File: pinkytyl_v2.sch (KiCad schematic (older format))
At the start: 62 parts, among them J1 50-00174, J2 Conn_01x02, J3 USB_B_Mini, J5 Conn_02x05_Odd_Even, K0 KEYSW, K10 KEYSW, K11 KEYSW, K12 KEYSW, K13 KEYSW, K14 KEYSW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

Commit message: Initial commit for chocs
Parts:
- added D1: D, Diode_SMD:D_SOD-123, symbol Device:D
- K0, K10, K11, K12, K13, K14, K15, K20, K21, K22, K23, K24, K25, K30, K31, K32, K33, K34, K35, K40, K41: footprint keyswitches:SW_MX_reversible_minimal -> keyswitches:SW_PG1350_reversible
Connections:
- net GND: now also U1.33 (~HWB~/PE2)
- net VCC: now also D1.1 (K); no longer J3.1 (VBUS), U1.7 (VBUS)
- new net UVCC: D1.2 (A), J3.1 (VBUS), U1.7 (VBUS)
- no-connect marks 20 -> 19
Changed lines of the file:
@@
-$EndComp
-$Comp
-L power:VCC #PWR0105
-U 1 1 614864FA
-P 2300 2000
-F 0 "#PWR0105" H 2300 1850 50  0001 C CNN
-F 1 "VCC" V 2300 2150 50  0000 L CNN
-F 2 "" H 2300 2000 50  0001 C CNN
-F 3 "" H 2300 2000 50  0001 C CNN
-	1    2300 2000
-	0    -1   -1   0
 $EndComp
 $Comp
@@
 NoConn ~ 3500 2900
 NoConn ~ 3500 3000
-NoConn ~ 3500 3300
 NoConn ~ 3500 3600
 NoConn ~ 3500 3700
@@
 F 0 "K10" H 5550 4133 60  0000 C CNN
 F 1 "KEYSW" H 5550 3800 60  0001 C CNN
-F 2 "keyswitches:SW_MX_reversible_minimal" H 5550 3900 60  0001 C CNN
+F 2 "keyswitches:SW_PG1350_reversible" H 5550 3900 60  0001 C CNN
 F 3 "" H 5550 3900 60  0000 C CNN
 	1    5550 3900
@@
 F 0 "K11" H 6450 4133 60  0000 C CNN
 F 1 "KEYSW" H 6450 3800 60  0001 C CNN
-F 2 "keyswitches:SW_MX_reversible_minimal" H 6450 3900 60  0001 C CNN
+F 2 "keyswitches:SW_PG1350_reversible" H 6450 3900 60  0001 C CNN
 F 3 "" H 6450 3900 60  0000 C CNN
 	1    6450 3900
@@
 F 0 "K12" H 7350 4133 60  0000 C CNN
 F 1 "KEYSW" H 7350 3800 60  0001 C CNN
-F 2 "keyswitches:SW_MX_reversible_minimal" H 7350 3900 60  0001 C CNN
+F 2 "keyswitches:SW_PG1350_reversible" H 7350 3900 60  0001 C CNN
 F 3 "" H 7350 3900 60  0000 C CNN
 	1    7350 3900
@@
 F 0 "K13" H 8200 4133 60  0000 C CNN
 F 1 "KEYSW" H 8200 3800 60  0001 C CNN
-F 2 "keyswitches:SW_MX_reversible_minimal" H 8200 3900 60  0001 C CNN
+F 2 "keyswitches:SW_PG1350_reversible" H 8200 3900 60  0001 C CNN
 F 3 "" H 8200 3900 60  0000 C CNN
 	1    8200 3900
@@
 F 0 "K14" H 9050 4133 60  0000 C CNN
 F 1 "KEYSW" H 9050 3800 60  0001 C CNN
-F 2 "keyswitches:SW_MX_reversible_minimal" H 9050 3900 60  0001 C CNN
+F 2 "keyswitches:SW_PG1350_reversible" H 9050 3900 60  0001 C CNN
 F 3 "" H 9050 3900 60  0000 C CNN
 	1    9050 3900
@@
 F 0 "K15" H 10000 4133 60  0000 C CNN
 F 1 "KEYSW" H 10000 3800 60  0001 C CNN
-F 2 "keyswitches:SW_MX_reversible_minimal" H 10000 3900 60  0001 C CNN
+F 2 "keyswitches:SW_PG1350_reversible" H 10000 3900 60  0001 C CNN
 F 3 "" H 10000 3900 60  0000 C CNN
 	1    10000 3900
@@
 F 0 "K20" H 5550 4883 60  0000 C CNN
 F 1 "KEYSW" H 5550 4550 60  0001 C CNN
-F 2 "keyswitches:SW_MX_reversible_minimal" H 5550 4650 60  0001 C CNN
+F 2 "keyswitches:SW_PG1350_reversible" H 5550 4650 60  0001 C CNN
 F 3 "" H 5550 4650 60  0000 C CNN
 	1    5550 4650
@@
 F 0 "K21" H 6450 4883 60  0000 C CNN
 F 1 "KEYSW" H 6450 4550 60  0001 C CNN
-F 2 "keyswitches:SW_MX_reversible_minimal" H 6450 4650 60  0001 C CNN
+F 2 "keyswitches:SW_PG1350_reversible" H 6450 4650 60  0001 C CNN
 F 3 "" H 6450 4650 60  0000 C CNN
 	1    6450 4650
@@
 F 0 "K22" H 7350 4883 60  0000 C CNN
 F 1 "KEYSW" H 7350 4550 60  0001 C CNN
-F 2 "keyswitches:SW_MX_reversible_minimal" H 7350 4650 60  0001 C CNN
+F 2 "keyswitches:SW_PG1350_reversible" H 7350 4650 60  0001 C CNN
 F 3 "" H 7350 4650 60  0000 C CNN
 	1    7350 4650
@@
 F 0 "K23" H 8200 4883 60  0000 C CNN
 F 1 "KEYSW" H 8200 4550 60  0001 C CNN
-F 2 "keyswitches:SW_MX_reversible_minimal" H 8200 4650 60  0001 C CNN
+F 2 "keyswitches:SW_PG1350_reversible" H 8200 4650 60  0001 C CNN
 F 3 "" H 8200 4650 60  0000 C CNN
 	1    8200 4650
@@
 F 0 "K24" H 9050 4883 60  0000 C CNN
 F 1 "KEYSW" H 9050 4550 60  0001 C CNN
-F 2 "keyswitches:SW_MX_reversible_minimal" H 9050 4650 60  0001 C CNN
+F 2 "keyswitches:SW_PG1350_reversible" H 9050 4650 60  0001 C CNN
 F 3 "" H 9050 4650 60  0000 C CNN
 	1    9050 4650
@@
 F 0 "K25" H 10000 4883 60  0000 C CNN
 F 1 "KEYSW" H 10000 4550 60  0001 C CNN
-F 2 "keyswitches:SW_MX_reversible_minimal" H 10000 4650 60  0001 C CNN
+F 2 "keyswitches:SW_PG1350_reversible" H 10000 4650 60  0001 C CNN
 F 3 "" H 10000 4650 60  0000 C CNN
 	1    10000 4650
@@
 F 0 "K30" H 5550 5683 60  0000 C CNN
 F 1 "KEYSW" H 5550 5350 60  0001 C CNN
-F 2 "keyswitches:SW_MX_reversible_minimal" H 5550 5450 60  0001 C CNN
+F 2 "keyswitches:SW_PG1350_reversible" H 5550 5450 60  0001 C CNN
 F 3 "" H 5550 5450 60  0000 C CNN
 	1    5550 5450
@@
 F 0 "K31" H 6450 5683 60  0000 C CNN
 F 1 "KEYSW" H 6450 5350 60  0001 C CNN
-F 2 "keyswitches:SW_MX_reversible_minimal" H 6450 5450 60  0001 C CNN
+F 2 "keyswitches:SW_PG1350_reversible" H 6450 5450 60  0001 C CNN
 F 3 "" H 6450 5450 60  0000 C CNN
 	1    6450 5450
@@
 F 0 "K32" H 7350 5683 60  0000 C CNN
 F 1 "KEYSW" H 7350 5350 60  0001 C CNN
-F 2 "keyswitches:SW_MX_reversible_minimal" H 7350 5450 60  0001 C CNN
+F 2 "keyswitches:SW_PG1350_reversible" H 7350 5450 60  0001 C CNN
 F 3 "" H 7350 5450 60  0000 C CNN
 	1    7350 5450
@@
 F 0 "K33" H 8200 5683 60  0000 C CNN
 F 1 "KEYSW" H 8200 5350 60  0001 C CNN
-F 2 "keyswitches:SW_MX_reversible_minimal" H 8200 5450 60  0001 C CNN
+F 2 "keyswitches:SW_PG1350_reversible" H 8200 5450 60  0001 C CNN
 F 3 "" H 8200 5450 60  0000 C CNN
 	1    8200 5450
@@
 F 0 "K34" H 9050 5683 60  0000 C CNN
 F 1 "KEYSW" H 9050 5350 60  0001 C CNN
-F 2 "keyswitches:SW_MX_reversible_minimal" H 9050 5450 60  0001 C CNN
+F 2 "keyswitches:SW_PG1350_reversible" H 9050 5450 60  0001 C CNN
 F 3 "" H 9050 5450 60  0000 C CNN
 	1    9050 5450
@@
 F 0 "K35" H 10000 5683 60  0000 C CNN
 F 1 "KEYSW" H 10000 5350 60  0001 C CNN
-F 2 "keyswitches:SW_MX_reversible_minimal" H 10000 5450 60  0001 C CNN
+F 2 "keyswitches:SW_PG1350_reversible" H 10000 5450 60  0001 C CNN
 F 3 "" H 10000 5450 60  0000 C CNN
 	1    10000 5450
@@
 F 0 "K40" H 9050 6383 60  0000 C CNN
 F 1 "KEYSW" H 9050 6050 60  0001 C CNN
-F 2 "keyswitches:SW_MX_reversible_minimal" H 9050 6150 60  0001 C CNN
+F 2 "keyswitches:SW_PG1350_reversible" H 9050 6150 60  0001 C CNN
 F 3 "" H 9050 6150 60  0000 C CNN
 	1    9050 6150
@@
 F 0 "K41" H 10000 6383 60  0000 C CNN
 F 1 "KEYSW" H 10000 6050 60  0001 C CNN
-F 2 "keyswitches:SW_MX_reversible_minimal" H 10000 6150 60  0001 C CNN
+F 2 "keyswitches:SW_PG1350_reversible" H 10000 6150 60  0001 C CNN
 F 3 "" H 10000 6150 60  0000 C CNN
 	1    10000 6150
@@
 F 0 "K0" H 6450 3483 60  0000 C CNN
 F 1 "KEYSW" H 6450 3150 60  0001 C CNN
-F 2 "keyswitches:SW_MX_reversible_minimal" H 6450 3250 60  0001 C CNN
+F 2 "keyswitches:SW_PG1350_reversible" H 6450 3250 60  0001 C CNN
 F 3 "" H 6450 3250 60  0000 C CNN
 	1    6450 3250
@@
 	1    0    0    -1
 $EndComp
-$Comp
-L power:VCC #PWR0109
-U 1 1 614BD830
-P 5350 850
-F 0 "#PWR0109" H 5350 700 50  0001 C CNN
-F 1 "VCC" V 5365 978 50  0000 L CNN
-F 2 "" H 5350 850 50  0001 C CNN
-F 3 "" H 5350 850 50  0001 C CNN
-	1    5350 850
-	0    1    1    0
-$EndComp
 NoConn ~ 5350 1250
 $Comp
@@
 Connection ~ 2900 800
 Wire Wire Line
-	2800 900  2800 800
-Wire Wire Line
-	2800 800  2900 800
-Wire Wire Line
 	950  1300 950  1200
 Connection ~ 950  1200
@@
 	1    0    0    -1
 $EndComp
+$Comp
+L power:GND #PWR06
+U 1 1 616DF351
+P 3500 3300
+F 0 "#PWR06" H 3500 3050 50  0001 C CNN
+F 1 "GND" V 3505 3172 50  0000 R CNN
+F 2 "" H 3500 3300 50  0001 C CNN
+F 3 "" H 3500 3300 50  0001 C CNN
+	1    3500 3300
+	0    -1   -1   0
+$EndComp
+$Comp
+L Device:D D1
+U 1 1 61713DAC
+P 5550 650
+F 0 "D1" H 5400 750 50  0000 L CNN
+F 1 "D" H 5595 730 50  0000 L CNN
+F 2 "Diode_SMD:D_SOD-123" H 5550 650 50  0001 C CNN
+F 3 "~" H 5550 650 50  0001 C CNN
+F 4 "C81598" H 5550 650 50  0001 C CNN "LCSC"
+	1    5550 650
+	-1   0    0    1
+$EndComp
+Text GLabel 5500 850  2    50   Input ~ 0
+UVCC
+Wire Wire Line
+	5500 850  5400 850
+Wire Wire Line
+	5400 650  5400 850
+Connection ~ 5400 850
+Wire Wire Line
+	5400 850  5350 850
+Wire Wire Line
+	2800 900  2800 800
+Wire Wire Line
+	2800 800  2900 800
+Text GLabel 2300 2000 0    50   Input ~ 0
+UVCC
+$Comp
+L power:VCC #PWR0105
+U 1 1 61762081
+P 5700 650
+F 0 "#PWR0105" H 5700 500 50  0001 C CNN
+F 1 "VCC" H 5715 823 50  0000 C CNN
+F 2 "" H 5700 650 50  0001 C CNN
+F 3 "" H 5700 650 50  0001 C CNN
+	1    5700 650
+	0    1    1    0
+$EndComp
 $EndSCHEMATC

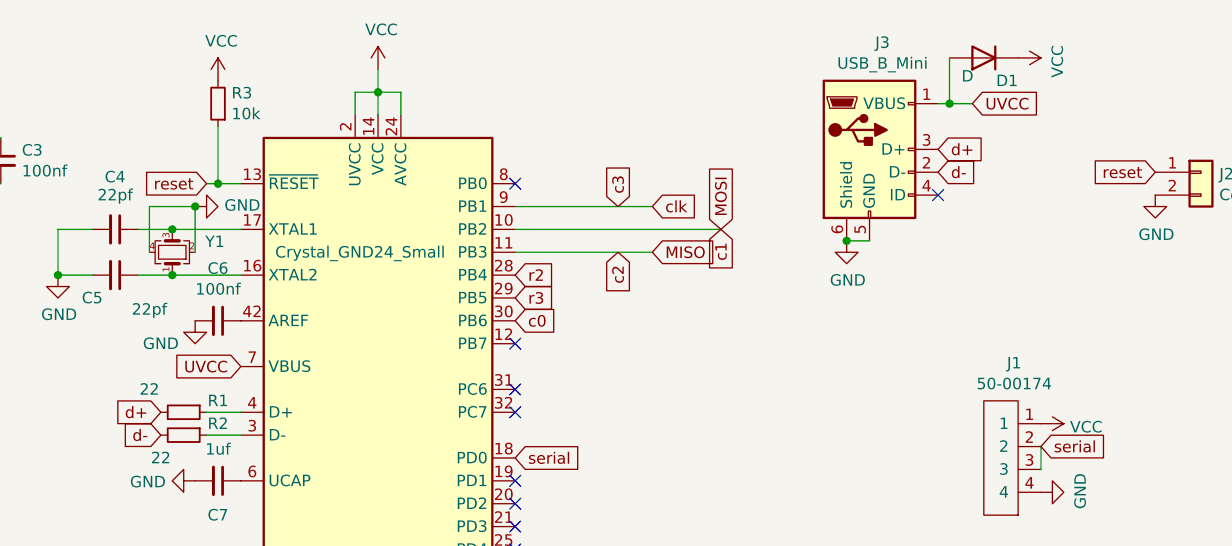
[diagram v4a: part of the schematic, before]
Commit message: Changed my mind regarding detection of VUSB, software solution is doing fine with less components
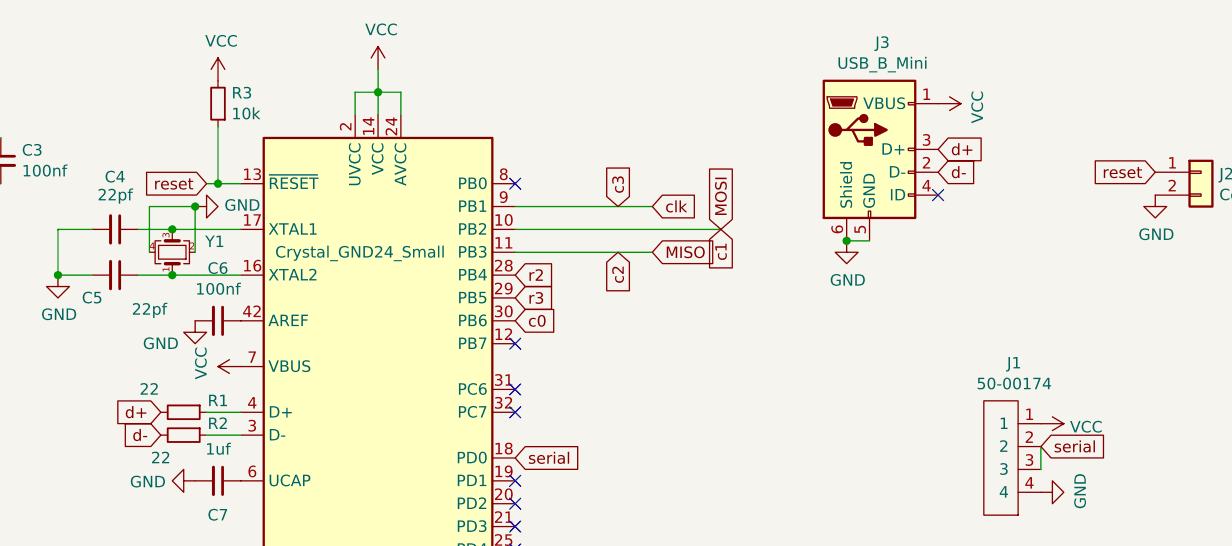
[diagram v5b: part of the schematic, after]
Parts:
- removed D1: D, Diode_SMD:D_SOD-123, symbol Device:D
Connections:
- net UVCC is gone; now on net VCC: J3.1 (VBUS), U1.7 (VBUS)
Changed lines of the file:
@@
 	0    -1   -1   0
 $EndComp
-$Comp
-L Device:D D1
-U 1 1 61713DAC
-P 5550 650
-F 0 "D1" H 5400 750 50  0000 L CNN
-F 1 "D" H 5595 730 50  0000 L CNN
-F 2 "Diode_SMD:D_SOD-123" H 5550 650 50  0001 C CNN
-F 3 "~" H 5550 650 50  0001 C CNN
-F 4 "C81598" H 5550 650 50  0001 C CNN "LCSC"
-	1    5550 650
-	-1   0    0    1
-$EndComp
-Text GLabel 5500 850  2    50   Input ~ 0
-UVCC
-Wire Wire Line
-	5500 850  5400 850
-Wire Wire Line
-	5400 650  5400 850
-Connection ~ 5400 850
-Wire Wire Line
-	5400 850  5350 850
 Wire Wire Line
 	2800 900  2800 800
 Wire Wire Line
 	2800 800  2900 800
-Text GLabel 2300 2000 0    50   Input ~ 0
-UVCC
 $Comp
 L power:VCC #PWR0105
 U 1 1 61762081
-P 5700 650
-F 0 "#PWR0105" H 5700 500 50  0001 C CNN
-F 1 "VCC" H 5715 823 50  0000 C CNN
-F 2 "" H 5700 650 50  0001 C CNN
-F 3 "" H 5700 650 50  0001 C CNN
-	1    5700 650
+P 5350 850
+F 0 "#PWR0105" H 5350 700 50  0001 C CNN
+F 1 "VCC" H 5365 1023 50  0000 C CNN
+F 2 "" H 5350 850 50  0001 C CNN
+F 3 "" H 5350 850 50  0001 C CNN
+	1    5350 850
 	0    1    1    0
 $EndComp
+$Comp
+L power:VCC #PWR0109
+U 1 1 618DF0A7
+P 2300 2000
+F 0 "#PWR0109" H 2300 1850 50  0001 C CNN
+F 1 "VCC" H 2315 2173 50  0000 C CNN
+F 2 "" H 2300 2000 50  0001 C CNN
+F 3 "" H 2300 2000 50  0001 C CNN
+	1    2300 2000
+	0    -1   -1   0
+$EndComp
 $EndSCHEMATC
